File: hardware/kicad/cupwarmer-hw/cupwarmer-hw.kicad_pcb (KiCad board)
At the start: 4 copper layers, 56 x 56 mm, 47 parts, among them J1 I2C Service, J3 STATUS_MON, Q1 AO3400 SOT-23, U1 STWLC38JRM

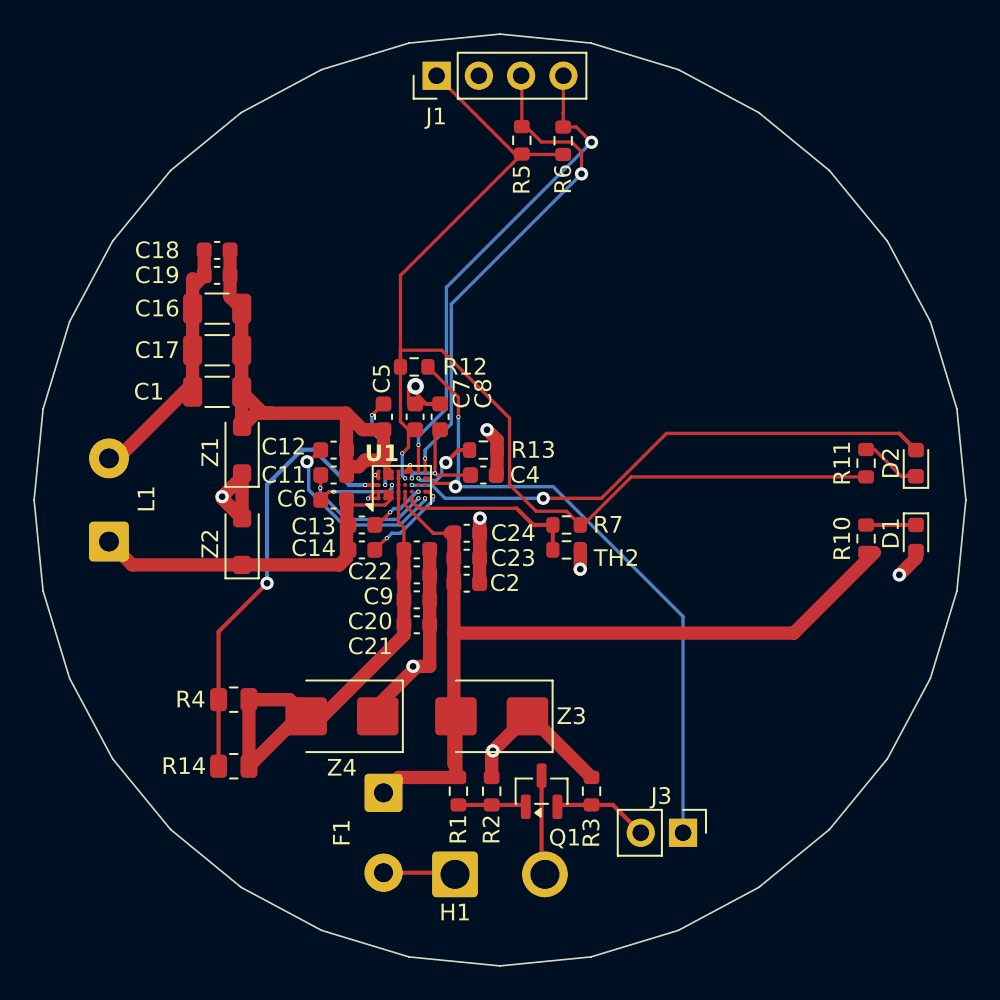
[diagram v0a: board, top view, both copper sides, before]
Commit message: Reposition U1 passives and add hole-to-hole DRC exclusions
Rotate and shift the COMA/COMB and Cs decoupling caps around U1, nudge
several breakout passives, and exclude a cluster of hole-to-hole DRC
violations under U1's BGA escape area where via spacing is intentional.
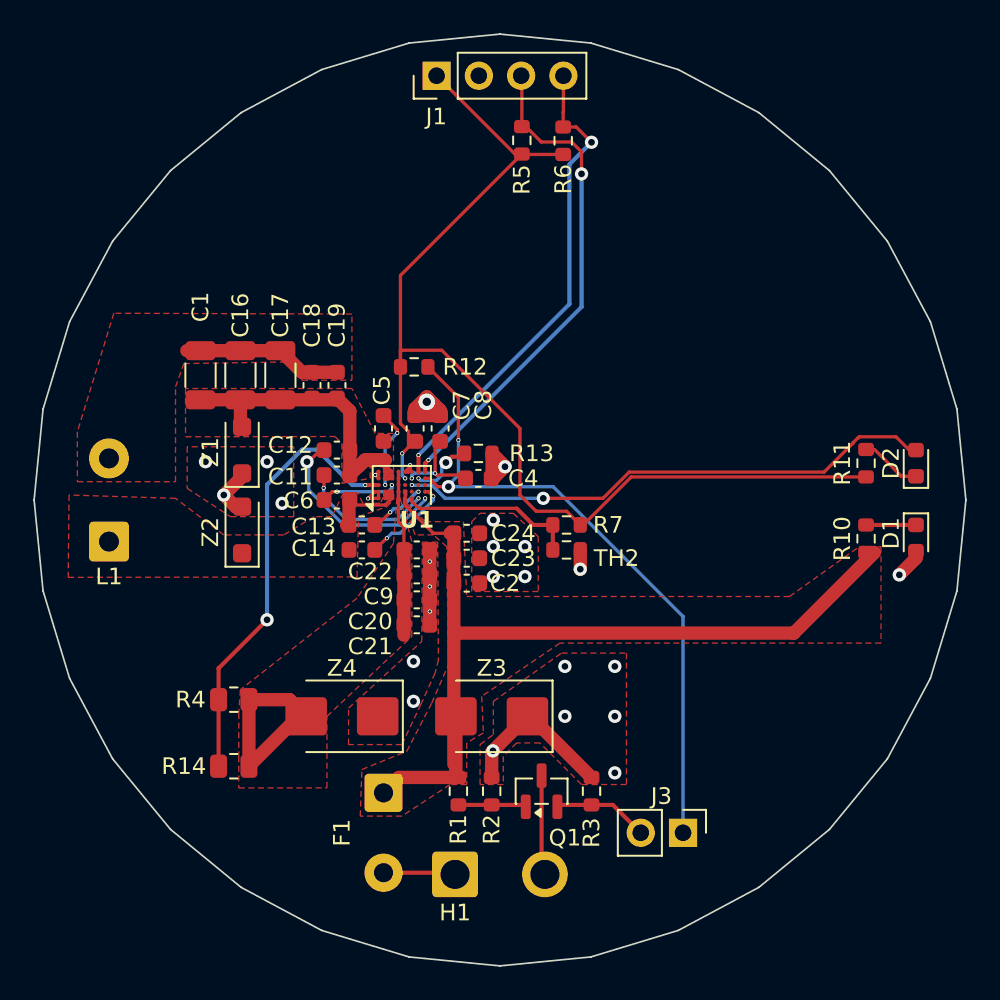
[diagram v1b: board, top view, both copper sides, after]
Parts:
- moved C18 9.90 mm to (88.7, 93.1), turned to -90 degrees
- moved C19 9.77 mm to (90.2, 93.1), turned to -90 degrees
- moved C16 4.24 mm to (84.4, 92.5), turned to -90 degrees
- moved C17 4.09 mm to (86.8, 92.5), turned to -90 degrees
- moved C1 1.41 mm to (82.0, 92.5), turned to -90 degrees
- moved C5 0.70 mm to (93.0, 95.7)
- moved C7 0.70 mm to (94.9, 95.7)
- moved C8 0.70 mm to (96.4, 95.7)
- moved Z2 0.70 mm to (84.5, 101.8)
- moved C4 0.36 mm to (98.7, 98.7)
- moved R13 0.36 mm to (98.7, 97.2)
- moved C11 0.20 mm to (90.2, 98.5)
- moved C12 0.20 mm to (90.2, 97.0)
- moved C6 0.20 mm to (90.2, 100.0)
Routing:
- net /rx-power/AC2: track 24.2 -> 7.00 mm
- net SYS_GND: track 49.4 -> 34.7 mm, vias 11 -> 27
- net /rx-power/AC1: track 33.9 -> 22.7 mm
- net /rx-power/VRECT: track 29.8 -> 22.9 mm
- net /rx-power/AC1 COIL: track 15.2 -> 9.76 mm
- net RX_VDD: track 6.56 -> 5.64 mm
- net /rx-power/BOOT1: track 5.51 -> 4.82 mm
- added copper zone on F.Cu, net /rx-power/AC1
- added copper zone on F.Cu, net /rx-power/AC1 COIL
- added copper zone on F.Cu, net /rx-power/AC2
- added copper zone on F.Cu, net /rx-power/VRECT
- added copper zone on F.Cu, net SYS_GND
- added copper zone on F.Cu, net VOUT_12V

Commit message: Rework SYS_GND segments around U1 and refresh DRC exclusions
Replace the SYS_GND stub routing under U1 with cleaner short segments,
nudge a couple of breakout pads, and refresh the hole-to-hole DRC
exclusion list to match the new via positions.
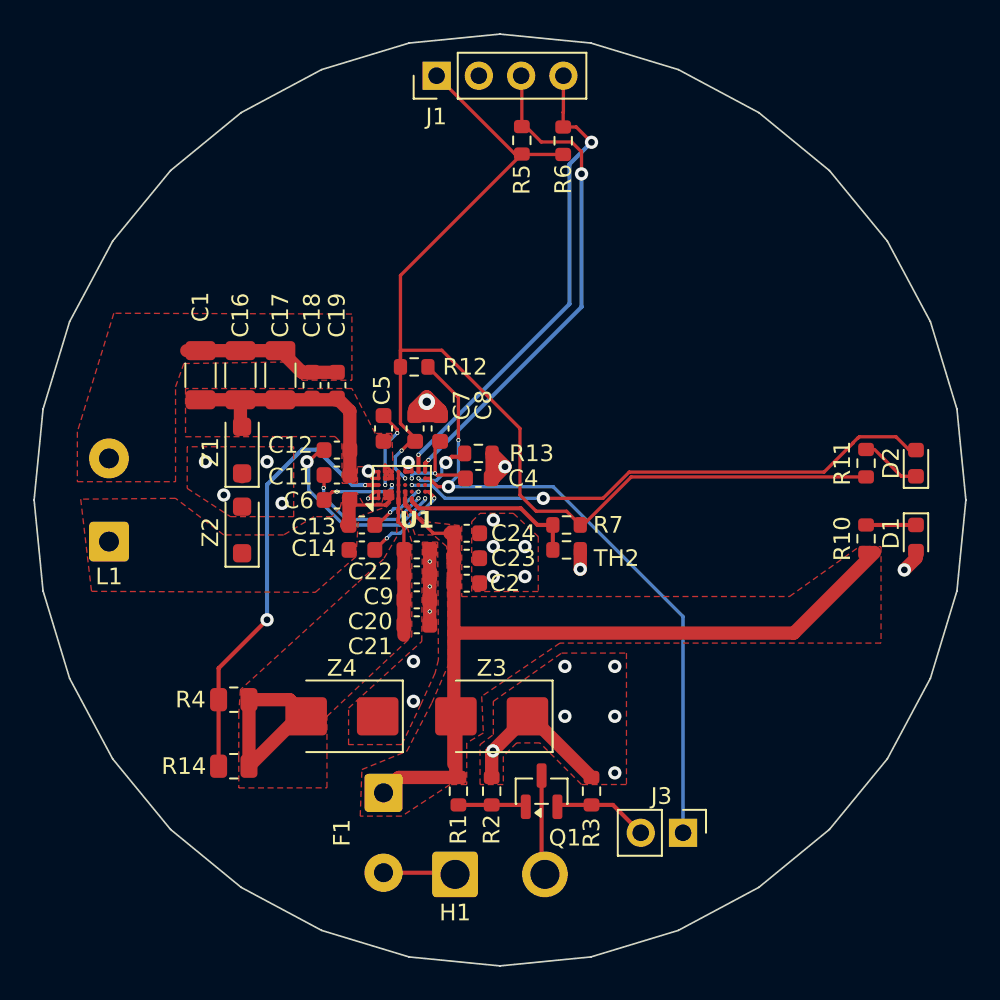
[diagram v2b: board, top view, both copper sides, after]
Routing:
- net /rx-power/AC1: track 22.7 -> 18.2 mm
- net SYS_GND: track 34.7 -> 32.8 mm
- net RX_VAA: track 69.2 -> 70.2 mm

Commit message: Replace coil/ferrite notes with BGA via fab note
Drop the placeholder "NO LARGE METAL OVER COIL CORE" and "FERRITE /
MECH ENVELOPE TBD" notes and add a Cmts.User note specifying that U1
BGA escape vias (0.15mm drill / 0.25mm dia) must be epoxy-filled and
copper-capped, with no open vias on BGA pads. Reposition the title
block.
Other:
- board text added: "U1 BGA escape vias: 0.15 mm drill / 0.25 mm diameter vias shall be epoxy-filled and copper-capped /plated over where located under or near U1 BGA pads. No open vias on BGA pads. Other component through-holes shall remain open and solderable."
- board text removed: "FERRITE / MECH ENVELOPE TBD"
- board text removed: "NO LARGE METAL OVER COIL CORE"
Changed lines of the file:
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@@
 		(layer "Edge.Cuts")
 	)
-	(gr_text "NO LARGE METAL\nOVER COIL CORE"
-		(at 126 77.5 0)
+	(gr_text "U1 BGA escape vias: 0.15 mm drill / 0.25 mm diameter vias shall be epoxy-filled and copper-capped /plated over\nwhere located under or near U1 BGA pads. No open vias on BGA pads.\nOther component through-holes shall remain open and solderable.\n"
+		(at 70.5 137.6 0)
 		(layer "Cmts.User")
 		(effects
 			(font
-				(size 1.1 1.1)
-				(thickness 0.14)
+				(size 1.5 1.5)
+				(thickness 0.3)
+				(bold yes)
 			)
-		)
-	)
-	(gr_text "FERRITE / MECH ENVELOPE TBD"
-		(at 100 132 0)
-		(layer "Cmts.User")
-		(effects
-			(font
-				(size 1.2 1.2)
-				(thickness 0.15)
-			)
+			(justify left bottom)
 		)
 	)
 	(gr_text "Cup Warmer Hardware\nInitial PCB scaffold\nTarget RX: STWLC38JRM"
-		(at 77.5 69 0)
+		(at 88.65 64.15 0)
 		(layer "Cmts.User")
 		(effects
